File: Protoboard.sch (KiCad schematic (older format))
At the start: 18 parts, among them P1 CONN_01X08, P2 CONN_01X04, P3 CONN_01X05, P4 CONN_01X11, P5 CONN_02X05

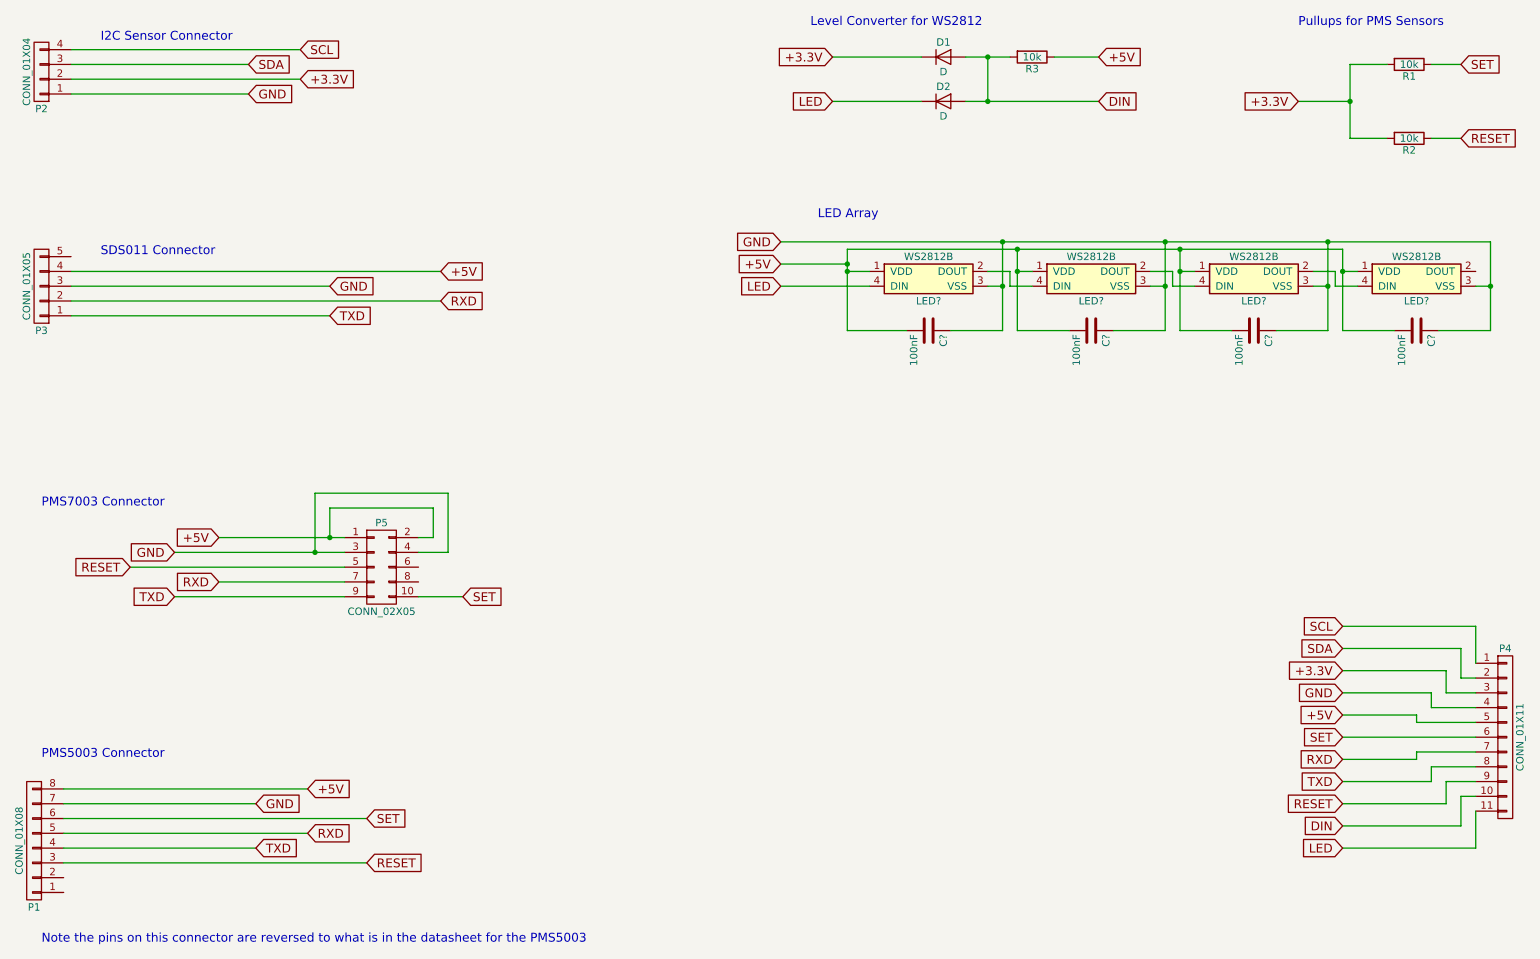
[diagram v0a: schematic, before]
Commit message: Routing and fill zones.
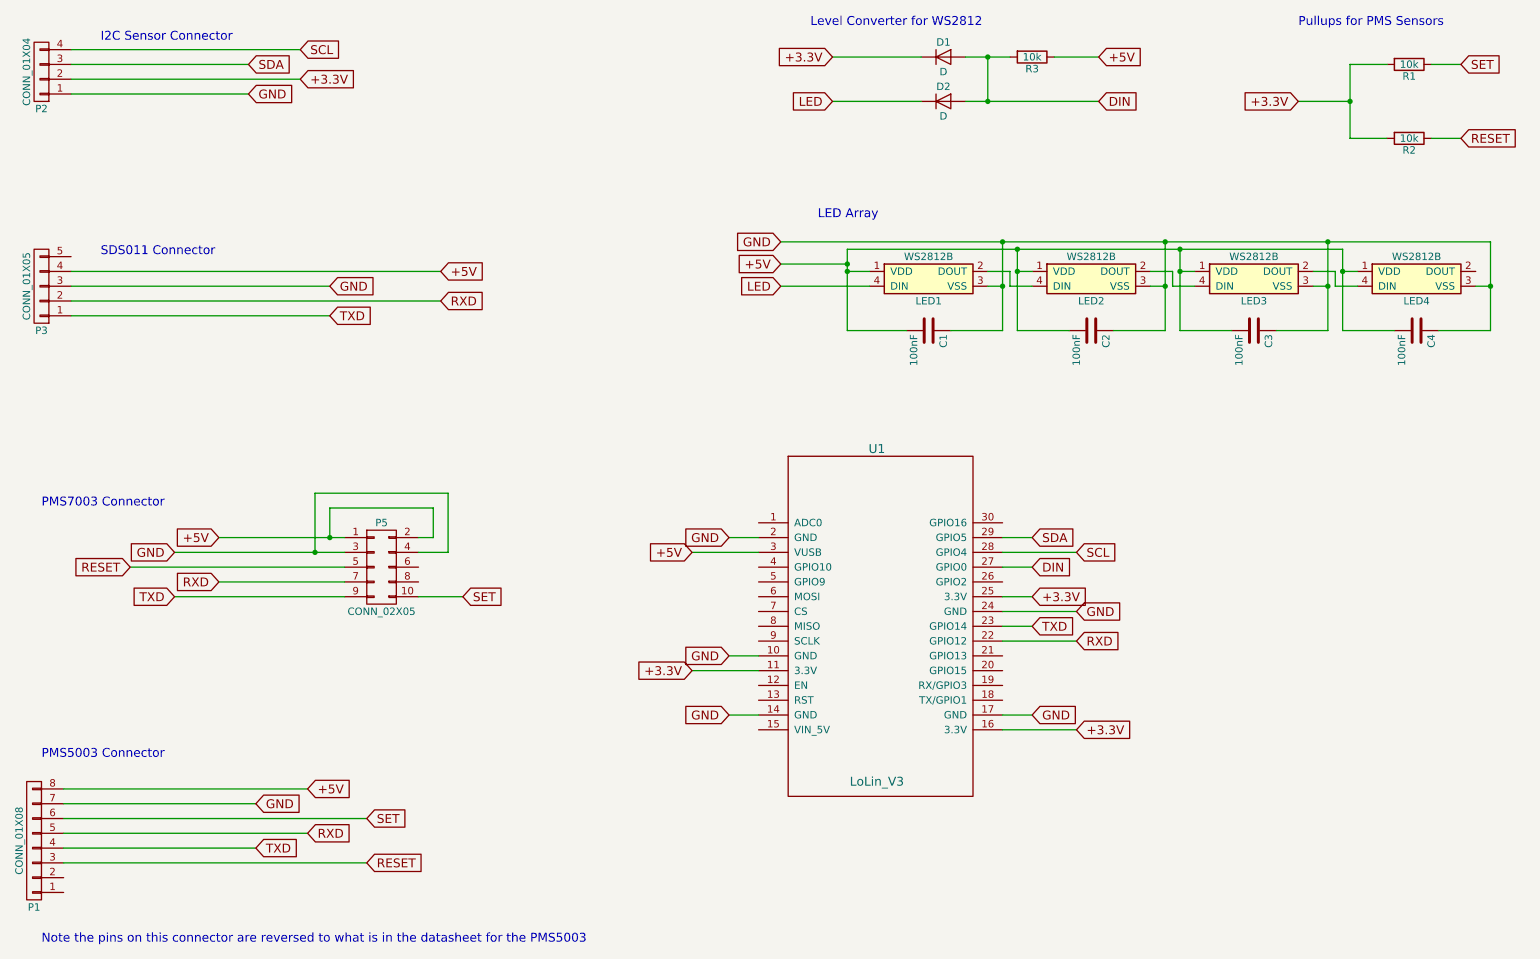
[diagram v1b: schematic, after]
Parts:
- removed P4: CONN_01X11, Pin_Headers:Pin_Header_Straight_1x11, symbol CONN_01X11
- added U1: LoLin_V3, LoLin:LoLin, symbol LoLin_V3
- C1, C2, C3, C4: renamed from C?; footprint (none) -> Capacitors_SMD:C_1206_HandSoldering
- P3: footprint Connectors_JST:JST_XH_B05B-XH-A_05x2.50mm_Straight -> Connectors_JST:JST_XH_S05B-XH-A_05x2.50mm_Angled
- gave numbers to parts that had none: 4
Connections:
- net +3.3V: now also U1.11 (3.3V), U1.16 (3.3V), U1.25 (3.3V)
- net +5V: now also U1.3 (VUSB)
- net DIN: now also U1.27 (GPIO0)
- net GND: now also U1.10 (GND), U1.14 (GND), U1.17 (GND), U1.2 (GND), U1.24 (GND)
- net RXD: now also U1.22 (GPIO12)
- net SCL: now also U1.28 (GPIO4)
- net SDA: now also U1.29 (GPIO5)
- net TXD: now also U1.23 (GPIO14)
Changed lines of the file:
@@
 LIBS:contrib
 LIBS:valves
+LIBS:leds
+LIBS:Worldsemi
 LIBS:lolin_v3
-LIBS:LoLin-cache
+LIBS:Protoboard-cache
 EELAYER 25 0
 EELAYER END
@@
 F 0 "P3" H 1000 2800 50  0000 C CNN
 F 1 "CONN_01X05" V 1100 2500 50  0000 C CNN
-F 2 "Connectors_JST:JST_XH_B05B-XH-A_05x2.50mm_Straight" H 1000 2500 50  0001 C CNN
+F 2 "Connectors_JST:JST_XH_S05B-XH-A_05x2.50mm_Angled" H 1000 2500 50  0001 C CNN
 F 3 "" H 1000 2500 50  0000 C CNN
 	1    1000 2500
@@
 Text Notes 6200 750  0    60   ~ 0
 Level Converter for WS2812\n
-Text GLabel 9800 4800 0    60   Input ~ 0
-SCL
-Text GLabel 9800 4950 0    60   Input ~ 0
-SDA
-Text GLabel 9800 5100 0    60   Input ~ 0
-+3.3V
-Text GLabel 9800 5400 0    60   Input ~ 0
-+5V
-Text GLabel 9800 5250 0    60   Input ~ 0
-GND
-Text GLabel 9800 5850 0    60   Input ~ 0
-TXD
-Text GLabel 9800 5700 0    60   Input ~ 0
-RXD
-Text GLabel 9800 5550 0    60   Input ~ 0
-SET
-Text GLabel 9800 6000 0    60   Input ~ 0
-RESET
-Text GLabel 9800 6150 0    60   Input ~ 0
-DIN
-Text GLabel 9800 6300 0    60   Input ~ 0
-LED
 Wire Wire Line
 	2400 1000 1200 1000
-$Comp
-L CONN_01X11 P4
-U 1 1 58C5C7BE
-P 10900 5550
-F 0 "P4" H 10900 6150 50  0000 C CNN
-F 1 "CONN_01X11" V 11000 5550 50  0000 C CNN
-F 2 "Pin_Headers:Pin_Header_Straight_1x11" H 10900 5550 50  0001 C CNN
-F 3 "" H 10900 5550 50  0000 C CNN
-	1    10900 5550
-	1    0    0    -1
-$EndComp
-Wire Wire Line
-	9800 4800 10700 4800
-Wire Wire Line
-	10700 4800 10700 5050
-Wire Wire Line
-	10700 5150 10600 5150
-Wire Wire Line
-	10600 5150 10600 4950
-Wire Wire Line
-	10600 4950 9800 4950
-Wire Wire Line
-	10700 5250 10500 5250
-Wire Wire Line
-	10500 5250 10500 5100
-Wire Wire Line
-	10500 5100 9800 5100
-Wire Wire Line
-	9800 5250 10400 5250
-Wire Wire Line
-	10400 5250 10400 5350
-Wire Wire Line
-	10400 5350 10700 5350
-Wire Wire Line
-	10700 5450 10300 5450
-Wire Wire Line
-	10300 5450 10300 5400
-Wire Wire Line
-	10300 5400 9800 5400
-Wire Wire Line
-	10700 5550 9800 5550
-Wire Wire Line
-	10700 5650 10300 5650
-Wire Wire Line
-	10300 5650 10300 5700
-Wire Wire Line
-	10300 5700 9800 5700
-Wire Wire Line
-	9800 5850 10400 5850
-Wire Wire Line
-	10400 5850 10400 5750
-Wire Wire Line
-	10400 5750 10700 5750
-Wire Wire Line
-	10700 5850 10500 5850
-Wire Wire Line
-	10500 5850 10500 6000
-Wire Wire Line
-	10500 6000 9800 6000
-Wire Wire Line
-	10700 5950 10600 5950
-Wire Wire Line
-	10600 5950 10600 6150
-Wire Wire Line
-	10600 6150 9800 6150
-Wire Wire Line
-	10700 6050 10700 6300
-Wire Wire Line
-	10700 6300 9800 6300
 Text Notes 1000 6950 0    60   ~ 0
 Note the pins on this connector are reversed to what is in the datasheet for the PMS5003\n
@@
 	2450 6000 1150 6000
 $Comp
-L WS2812B LED?
+L WS2812B LED1
 U 1 1 58DEC565
 P 7000 2400
-F 0 "LED?" H 7000 2200 50  0000 C CNN
+F 0 "LED1" H 7000 2200 50  0000 C CNN
 F 1 "WS2812B" H 7000 2500 50  0000 C CNN
 F 2 "LEDs:LED_WS2812B-PLCC4" H 7000 2100 50  0001 C CNN
@@
 $EndComp
 $Comp
-L WS2812B LED?
+L WS2812B LED4
 U 1 1 58DEC5E0
 P 10300 2400
-F 0 "LED?" H 10300 2200 50  0000 C CNN
+F 0 "LED4" H 10300 2200 50  0000 C CNN
 F 1 "WS2812B" H 10300 2500 50  0000 C CNN
 F 2 "LEDs:LED_WS2812B-PLCC4" H 10300 2100 50  0001 C CNN
@@
 $EndComp
 $Comp
-L WS2812B LED?
+L WS2812B LED2
 U 1 1 58DEC633
 P 8100 2400
-F 0 "LED?" H 8100 2200 50  0000 C CNN
+F 0 "LED2" H 8100 2200 50  0000 C CNN
 F 1 "WS2812B" H 8100 2500 50  0000 C CNN
 F 2 "LEDs:LED_WS2812B-PLCC4" H 8100 2100 50  0001 C CNN
@@
 $EndComp
 $Comp
-L WS2812B LED?
+L WS2812B LED3
 U 1 1 58DEC681
 P 9200 2400
-F 0 "LED?" H 9200 2200 50  0000 C CNN
+F 0 "LED3" H 9200 2200 50  0000 C CNN
 F 1 "WS2812B" H 9200 2500 50  0000 C CNN
 F 2 "LEDs:LED_WS2812B-PLCC4" H 9200 2100 50  0001 C CNN
@@
 $EndComp
 $Comp
-L C C?
+L C C1
 U 1 1 58DECC52
 P 7000 2800
-F 0 "C?" H 7025 2900 50  0000 L CNN
+F 0 "C1" H 7025 2900 50  0000 L CNN
 F 1 "100nF" H 7025 2700 50  0000 L CNN
-F 2 "" H 7038 2650 50  0001 C CNN
+F 2 "Capacitors_SMD:C_1206_HandSoldering" H 7038 2650 50  0001 C CNN
 F 3 "" H 7000 2800 50  0001 C CNN
 	1    7000 2800
@@
 $EndComp
 $Comp
-L C C?
+L C C2
 U 1 1 58DECCBA
 P 8100 2800
-F 0 "C?" H 8125 2900 50  0000 L CNN
+F 0 "C2" H 8125 2900 50  0000 L CNN
 F 1 "100nF" H 8125 2700 50  0000 L CNN
-F 2 "" H 8138 2650 50  0001 C CNN
+F 2 "Capacitors_SMD:C_1206_HandSoldering" H 8138 2650 50  0001 C CNN
 F 3 "" H 8100 2800 50  0001 C CNN
 	1    8100 2800
@@
 $EndComp
 $Comp
-L C C?
+L C C3
 U 1 1 58DECD22
 P 9200 2800
-F 0 "C?" H 9225 2900 50  0000 L CNN
+F 0 "C3" H 9225 2900 50  0000 L CNN
 F 1 "100nF" H 9225 2700 50  0000 L CNN
-F 2 "" H 9238 2650 50  0001 C CNN
+F 2 "Capacitors_SMD:C_1206_HandSoldering" H 9238 2650 50  0001 C CNN
 F 3 "" H 9200 2800 50  0001 C CNN
 	1    9200 2800
@@
 $EndComp
 $Comp
-L C C?
+L C C4
 U 1 1 58DECD93
 P 10300 2800
-F 0 "C?" H 10325 2900 50  0000 L CNN
+F 0 "C4" H 10325 2900 50  0000 L CNN
 F 1 "100nF" H 10325 2700 50  0000 L CNN
-F 2 "" H 10338 2650 50  0001 C CNN
+F 2 "Capacitors_SMD:C_1206_HandSoldering" H 10338 2650 50  0001 C CNN
 F 3 "" H 10300 2800 50  0001 C CNN
 	1    10300 2800
@@
 Text Notes 6250 2050 0    60   ~ 0
 LED Array\n
+$Comp
+L LoLin_V3 U1
+U 1 1 58DECC07
+P 6050 3650
+F 0 "U1" H 6650 3700 60  0000 C CNN
+F 1 "LoLin_V3" H 6650 1450 60  0000 C CNN
+F 2 "LoLin:LoLin" H 7000 2850 60  0001 C CNN
+F 3 "" H 7000 2850 60  0000 C CNN
+	1    6050 3650
+	1    0    0    -1
+$EndComp
+Text GLabel 5650 4200 0    60   Input ~ 0
+GND
+Text GLabel 5400 4300 0    60   Input ~ 0
++5V
+Text GLabel 7700 4200 2    60   Input ~ 0
+SDA
+Text GLabel 8000 4300 2    60   Input ~ 0
+SCL
+Text GLabel 7700 4400 2    60   Input ~ 0
+DIN
+Text GLabel 7700 4800 2    60   Input ~ 0
+TXD
+Text GLabel 8000 4900 2    60   Input ~ 0
+RXD
+Text GLabel 8000 4700 2    60   Input ~ 0
+GND
+Text GLabel 7700 4600 2    60   Input ~ 0
++3.3V
+Wire Wire Line
+	5650 4200 5850 4200
+Wire Wire Line
+	5850 4300 5400 4300
+Wire Wire Line
+	7500 4200 7700 4200
+Wire Wire Line
+	7500 4300 8000 4300
+Wire Wire Line
+	7700 4400 7500 4400
+Wire Wire Line
+	7500 4600 7700 4600
+Wire Wire Line
+	7500 4700 8000 4700
+Wire Wire Line
+	7700 4800 7500 4800
+Wire Wire Line
+	7500 4900 8000 4900
+Text GLabel 5400 5100 0    60   Input ~ 0
++3.3V
+Text GLabel 5650 5000 0    60   Input ~ 0
+GND
+Text GLabel 7700 5400 2    60   Input ~ 0
+GND
+Text GLabel 8000 5500 2    60   Input ~ 0
++3.3V
+Wire Wire Line
+	7700 5400 7500 5400
+Wire Wire Line
+	7500 5500 8000 5500
+Wire Wire Line
+	5650 5000 5850 5000
+Wire Wire Line
+	5850 5100 5400 5100
+Text GLabel 5650 5400 0    60   Input ~ 0
+GND
+Wire Wire Line
+	5650 5400 5850 5400
 $EndSCHEMATC

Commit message: Removed gerber files.
This is rev 2
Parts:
- removed D1, D2: D, Diodes_SMD:SOD-323_HandSoldering, symbol D
- added Q1: 2N7000, TO_SOT_Packages_THT:TO-92_Inline_Wide, symbol Q_NMOS_SGD
- added R4: 10k, Resistors_THT:Resistor_Horizontal_RM7mm, symbol R
- R1, R2, R3: footprint Resistors_SMD:R_1206_HandSoldering -> Resistors_THT:Resistor_Horizontal_RM7mm
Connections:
- net +3.3V: now also P2.1 (P1), R3.1, Q1.2 (G); no longer P2.2 (P2)
- net +5V: now also R4.1; no longer R3.1
- net DIN: now also Q1.1 (S)
- net GND: now also P2.2 (P2); no longer P2.1 (P1)
- net LED: now also Q1.3 (D), R4.2
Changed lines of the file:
@@
 	-1   0    0    1
 $EndComp
+Text GLabel 2750 1100 2    60   Input ~ 0
+GND
 Text GLabel 2400 1200 2    60   Input ~ 0
-GND
-Text GLabel 2750 1100 2    60   Input ~ 0
 +3.3V
 Text GLabel 2400 1000 2    60   Input ~ 0
@@
 F 0 "R2" V 10330 1500 50  0000 C CNN
 F 1 "10k" V 10250 1500 50  0000 C CNN
-F 2 "Resistors_SMD:R_1206_HandSoldering" V 10180 1500 50  0001 C CNN
+F 2 "Resistors_THT:Resistor_Horizontal_RM7mm" V 10180 1500 50  0001 C CNN
 F 3 "" H 10250 1500 50  0000 C CNN
 	1    10250 1500
@@
 F 0 "R1" V 10330 1000 50  0000 C CNN
 F 1 "10k" V 10250 1000 50  0000 C CNN
-F 2 "Resistors_SMD:R_1206_HandSoldering" V 10180 1000 50  0001 C CNN
+F 2 "Resistors_THT:Resistor_Horizontal_RM7mm" V 10180 1000 50  0001 C CNN
 F 3 "" H 10250 1000 50  0000 C CNN
 	1    10250 1000
@@
 Text Notes 9500 750  0    60   ~ 0
 Pullups for PMS Sensors\n
-$Comp
-L D D1
-U 1 1 58C46C46
-P 7100 950
-F 0 "D1" H 7100 1050 50  0000 C CNN
-F 1 "D" H 7100 850 50  0000 C CNN
-F 2 "Diodes_SMD:SOD-323_HandSoldering" H 7100 950 50  0001 C CNN
-F 3 "" H 7100 950 50  0000 C CNN
-	1    7100 950
-	1    0    0    -1
-$EndComp
-$Comp
-L D D2
-U 1 1 58C46CBC
-P 7100 1250
-F 0 "D2" H 7100 1350 50  0000 C CNN
-F 1 "D" H 7100 1150 50  0000 C CNN
-F 2 "Diodes_SMD:SOD-323_HandSoldering" H 7100 1250 50  0001 C CNN
-F 3 "" H 7100 1250 50  0000 C CNN
-	1    7100 1250
-	1    0    0    -1
-$EndComp
-Text GLabel 8150 1250 2    60   Input ~ 0
+Text GLabel 6350 1350 0    60   Input ~ 0
 DIN
 Text GLabel 8150 950  2    60   Input ~ 0
 +5V
-$Comp
-L R R3
-U 1 1 58C46D88
-P 7700 950
-F 0 "R3" V 7780 950 50  0000 C CNN
-F 1 "10k" V 7700 950 50  0000 C CNN
-F 2 "Resistors_SMD:R_1206_HandSoldering" V 7630 950 50  0001 C CNN
-F 3 "" H 7700 950 50  0000 C CNN
-	1    7700 950
-	0    1    1    0
-$EndComp
-Wire Wire Line
-	7850 950  8150 950
-Wire Wire Line
-	7550 950  7250 950
-Wire Wire Line
-	7250 1250 8150 1250
 Text GLabel 6350 950  0    60   Input ~ 0
 +3.3V
-Wire Wire Line
-	6350 950  6950 950
-Text GLabel 6350 1250 0    60   Input ~ 0
+Text GLabel 8150 1350 2    60   Input ~ 0
 LED
-Wire Wire Line
-	6350 1250 6950 1250
 Text Notes 6200 750  0    60   ~ 0
 Level Converter for WS2812\n
@@
 	6000 2350 6450 2350
 Connection ~ 6450 2350
-Wire Wire Line
-	7400 1250 7400 950
-Connection ~ 7400 950
-Connection ~ 7400 1250
 Text Notes 6250 2050 0    60   ~ 0
 LED Array\n
@@
 Wire Wire Line
 	5650 5400 5850 5400
+$Comp
+L R R3
+U 1 1 58E6A6D5
+P 6600 1150
+F 0 "R3" V 6680 1150 50  0000 C CNN
+F 1 "10k" V 6600 1150 50  0000 C CNN
+F 2 "Resistors_THT:Resistor_Horizontal_RM7mm" V 6530 1150 50  0001 C CNN
+F 3 "" H 6600 1150 50  0001 C CNN
+	1    6600 1150
+	1    0    0    -1
+$EndComp
+$Comp
+L R R4
+U 1 1 58E6A736
+P 7850 1150
+F 0 "R4" V 7930 1150 50  0000 C CNN
+F 1 "10k" V 7850 1150 50  0000 C CNN
+F 2 "Resistors_THT:Resistor_Horizontal_RM7mm" V 7780 1150 50  0001 C CNN
+F 3 "" H 7850 1150 50  0001 C CNN
+	1    7850 1150
+	1    0    0    -1
+$EndComp
+Wire Wire Line
+	6350 950  7250 950
+Wire Wire Line
+	6600 1000 6600 950
+Connection ~ 6600 950
+Wire Wire Line
+	6350 1350 7050 1350
+Wire Wire Line
+	6600 1350 6600 1300
+Connection ~ 6600 1350
+Wire Wire Line
+	7450 1350 8150 1350
+Wire Wire Line
+	7850 1350 7850 1300
+Connection ~ 7850 1350
+Wire Wire Line
+	8150 950  7850 950
+Wire Wire Line
+	7850 950  7850 1000
+$Comp
+L Q_NMOS_SGD Q1
+U 1 1 58E6BCFB
+P 7250 1250
+F 0 "Q1" H 7450 1300 50  0000 L CNN
+F 1 "2N7000" H 7450 1200 50  0000 L CNN
+F 2 "TO_SOT_Packages_THT:TO-92_Inline_Wide" H 7450 1350 50  0001 C CNN
+F 3 "" H 7250 1250 50  0001 C CNN
+	1    7250 1250
+	0    1    1    0
+$EndComp
+Wire Wire Line
+	7250 950  7250 1050
 $EndSCHEMATC
